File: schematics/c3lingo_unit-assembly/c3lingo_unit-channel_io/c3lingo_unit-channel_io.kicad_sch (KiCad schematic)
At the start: 40 parts, among them J601 Mic X In, J602 Headphone X, J603 Interconnect, J604 PowerSupply, J605 PhantomPower, U601 NE5534, U602 TPA6111A2

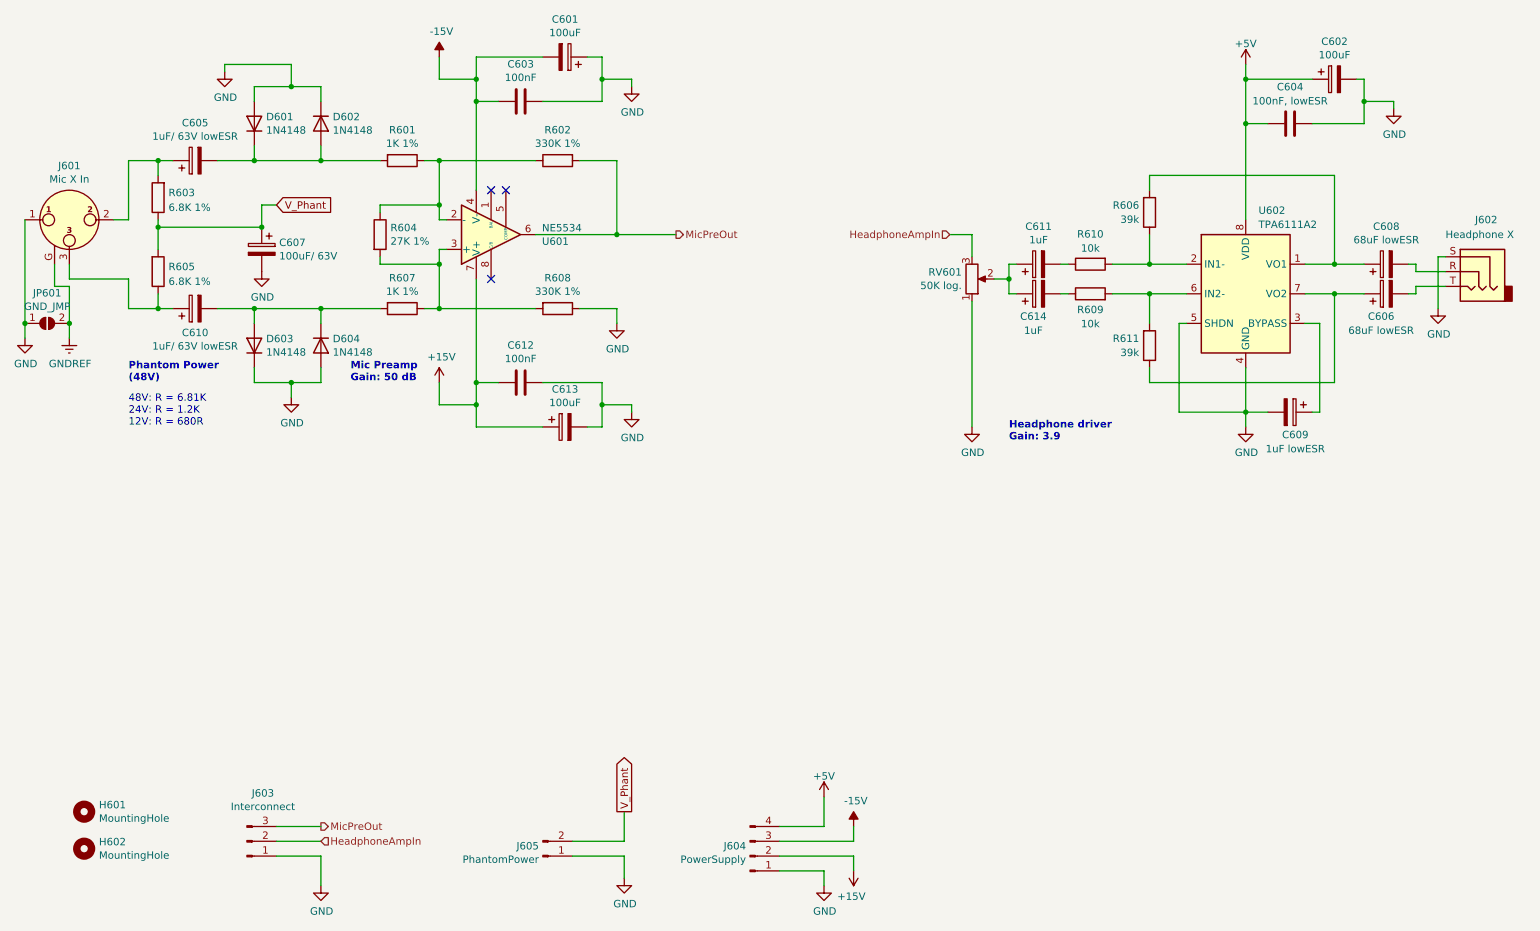
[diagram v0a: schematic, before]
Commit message: Reworks board-to-board connections
Instead of having connections between all boards, use the mix_io board as an audio signal distribution hub.

Note: PCB not updated
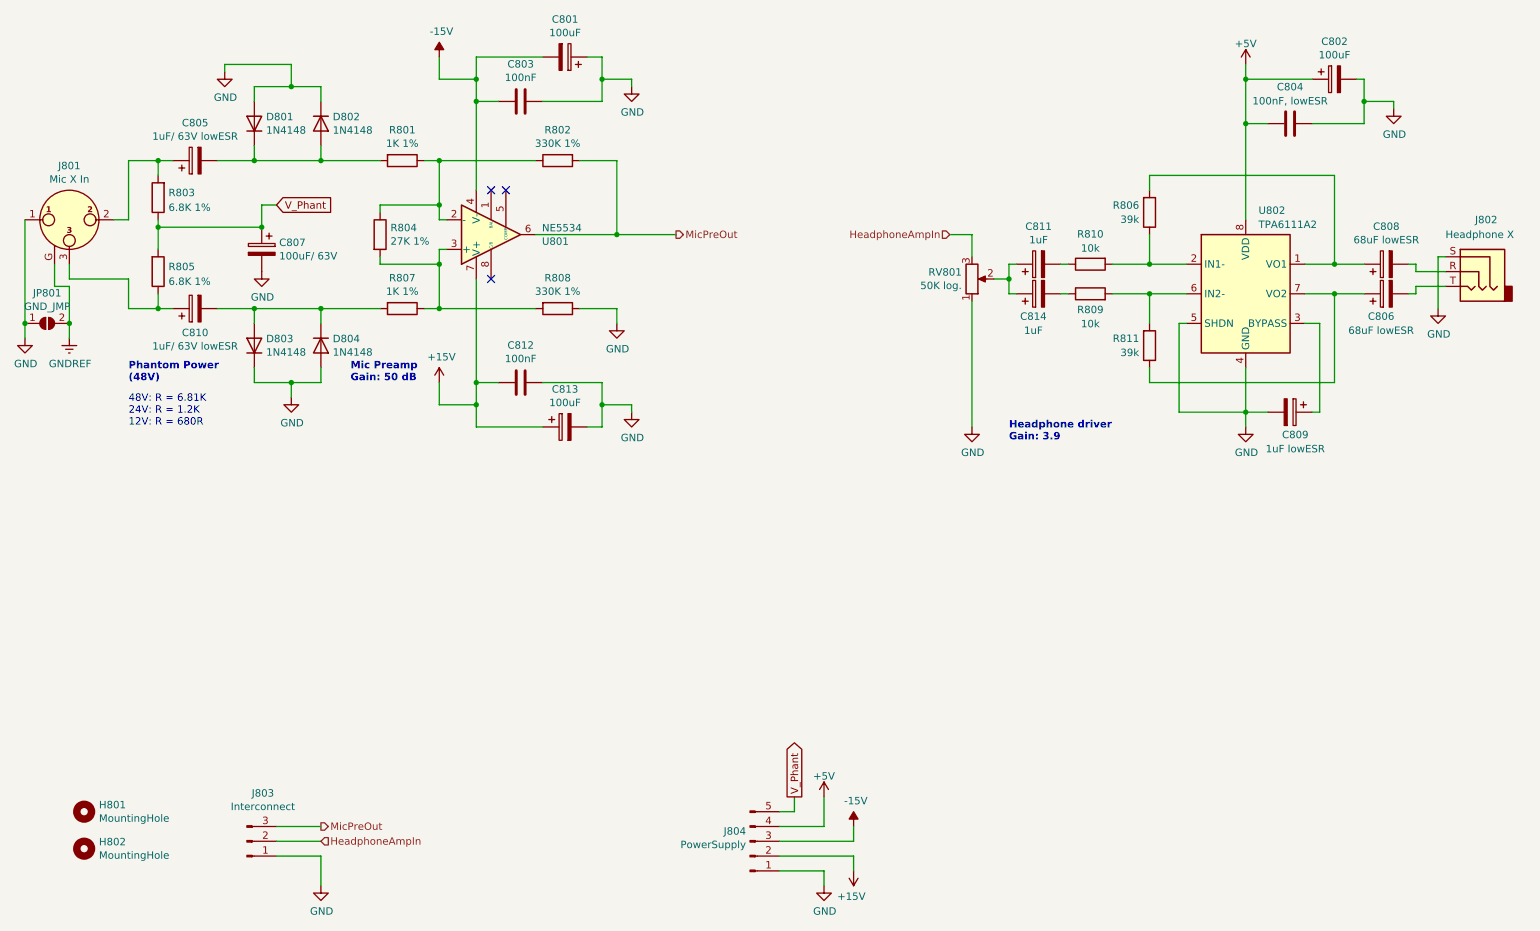
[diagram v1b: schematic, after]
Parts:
- removed J605: PhantomPower, TerminalBlock_Phoenix:TerminalBlock_Phoenix_PTSM-0,5-2-2.5-H-THR_1x02_P2.50mm_Horizontal, symbol Connector:Conn_01x02_Pin
- J803: renamed from J603; footprint TerminalBlock_Phoenix:TerminalBlock_Phoenix_PTSM-0,5-3-2.5-H-THR_1x03_P2.50mm_Horizontal -> TerminalBlock_Phoenix:TerminalBlock_Phoenix_PTSM-0,5-3-2.5-V-THR_1x03_P2.50mm_Vertical; Model PTSM 0,5/ 3-2,5-H THR -> PTSM 0,5/ 3-2,5-V THR
- J804: renamed from J604; footprint TerminalBlock_Phoenix:TerminalBlock_Phoenix_PTSM-0,5-4-2.5-H-THR_1x04_P2.50mm_Horizontal -> TerminalBlock_Phoenix:TerminalBlock_Phoenix_PTSM-0,5-5-2.5-V-THR_1x05_P2.50mm_Vertical; symbol Connector:Conn_01x04_Pin -> Connector:Conn_01x05_Pin; Model PTSM 0,5/ 4-2,5-H THR -> PTSM 0,5/ 5-2,5-V THR
- renumbered C601 to C801, C602 to C802, C603 to C803, C604 to C804, C605 to C805, C606 to C806, C607 to C807, C608 to C808, C609 to C809, C610 to C810, C611 to C811, C612 to C812, C613 to C813, C614 to C814, D601 to D801, D602 to D802, D603 to D803, D604 to D804, H601 to H801, H602 to H802, J601 to J801, J602 to J802, JP601 to JP801, R601 to R801, R602 to R802, R603 to R803, R604 to R804, R605 to R805, R606 to R806, R607 to R807, R608 to R808, R609 to R809, R610 to R810, R611 to R811, RV601 to RV801, U601 to U801, U602 to U802
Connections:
- net V_Phant: now also J804.5 (Pin_5)

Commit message: Re-layout boards with SMD components
* Channel Mix: Removed vu meter potentiometer as good setting was found (10 dB
  more headroom)
* Channel Mix: Add vu meter alternate power
* Channel I/O: Added jumper for phantom power enable/disable
* Add GND test points
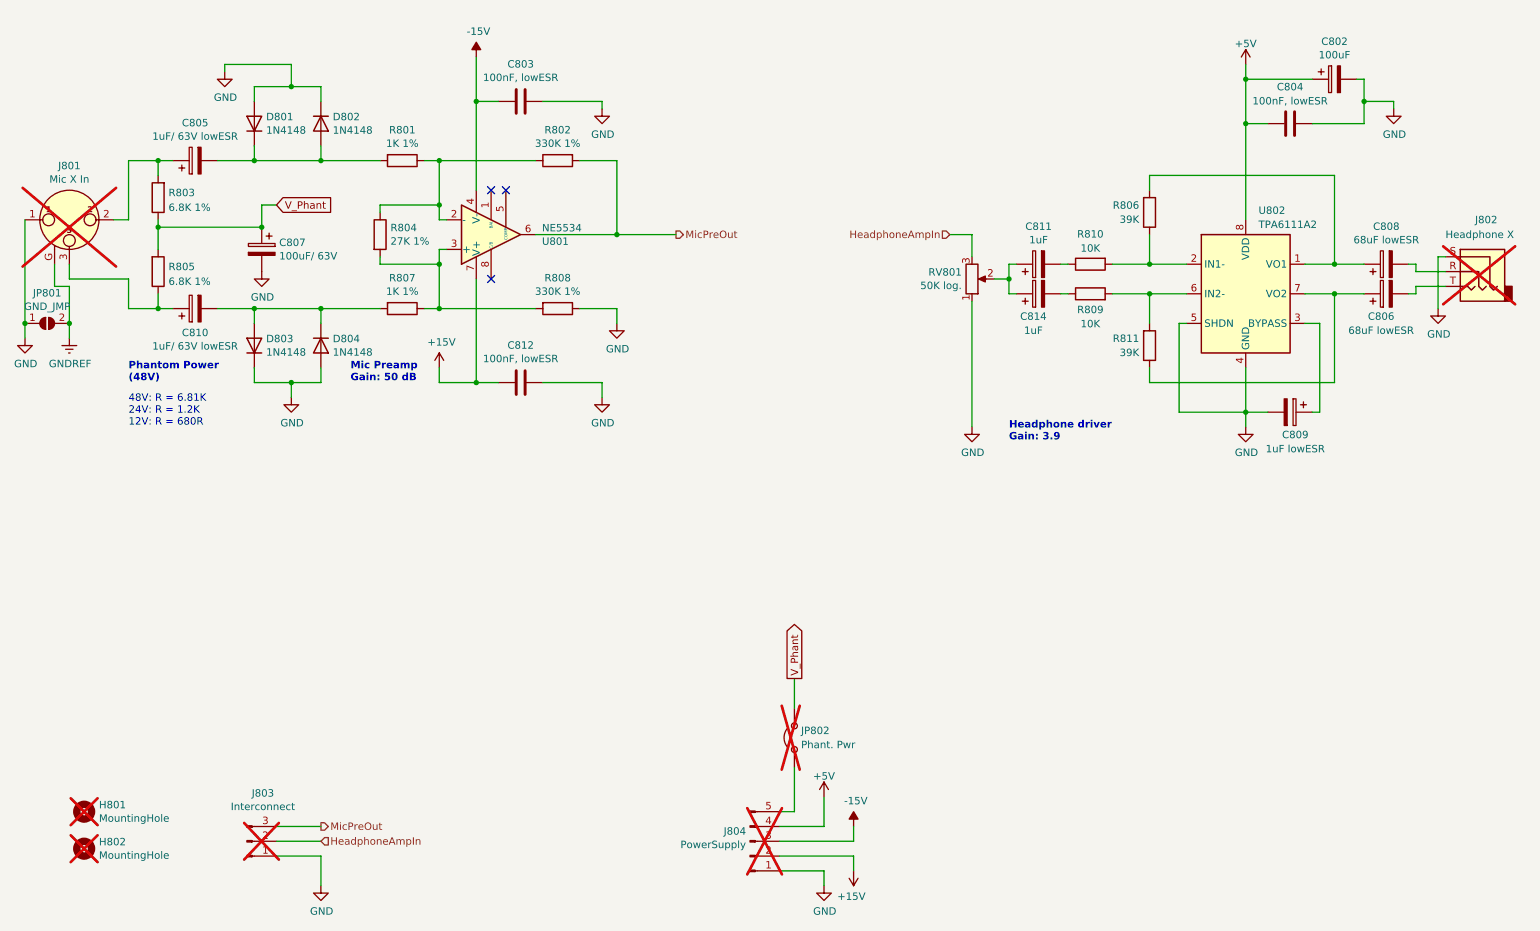
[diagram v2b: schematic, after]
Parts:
- removed C801, C813: 100uF, Capacitor_THT:CP_Radial_D6.3mm_P2.50mm, symbol Device:C_Polarized
- added JP802: Phant. Pwr, Connector_PinHeader_2.54mm:PinHeader_1x02_P2.54mm_Vertical, symbol Jumper:Jumper_2_Open
- C802: footprint Capacitor_THT:CP_Radial_D6.3mm_P2.50mm -> Capacitor_SMD:C_Elec_6.3x7.7; LCSC Part # (none) -> C72478; Model (none) -> 25V+
- C803, C812: value 100nF -> 100nF, lowESR; footprint Capacitor_THT:C_Disc_D5.0mm_W2.5mm_P5.00mm -> Capacitor_SMD:C_0603_1608Metric_Pad1.08x0.95mm_HandSolder; LCSC Part # (none) -> C14663; Model (none) -> 25V+
- C804: footprint Capacitor_THT:C_Disc_D5.0mm_W2.5mm_P5.00mm -> Capacitor_SMD:C_0603_1608Metric_Pad1.08x0.95mm_HandSolder; LCSC Part # (none) -> C14663; Model (none) -> 25V+
- C805, C810, C811, C814: footprint Capacitor_THT:CP_Radial_D5.0mm_P2.00mm -> Capacitor_SMD:C_Elec_4x5.8; LCSC Part # (none) -> C336256
- C806, C808: footprint Capacitor_THT:CP_Radial_D6.3mm_P2.50mm -> Capacitor_SMD:C_Elec_6.3x5.8; LCSC Part # (none) -> C72478
- C807: footprint Capacitor_THT:CP_Radial_D10.0mm_P5.00mm -> Capacitor_SMD:C_Elec_6.3x7.7; LCSC Part # (none) -> C72478
- C809: footprint Capacitor_THT:C_Disc_D5.0mm_W2.5mm_P5.00mm -> Capacitor_SMD:C_Elec_4x5.8; LCSC Part # (none) -> C336256
- D801, D802, D803, D804: footprint Diode_THT:D_DO-35_SOD27_P10.16mm_Horizontal -> Diode_SMD:D_SOD-123; LCSC Part # (none) -> C7420318; Model (none) -> 1N4148W (SOD-123)
- H801, H802: now not fitted; now left out of the parts list
- J801: Model NC3FAAH2 (Horiz. Male) -> NC3FAAH2 (Horiz. Female); now not fitted
- J802, J803, J804: now not fitted
- JP801: now left out of the parts list
- R801, R802, R803, R804, R805, R807, R808: footprint Resistor_THT:R_Axial_DIN0207_L6.3mm_D2.5mm_P10.16mm_Horizontal -> Resistor_SMD:R_0805_2012Metric_Pad1.20x1.40mm_HandSolder
- R806, R811: value 39k -> 39K; footprint Resistor_THT:R_Axial_DIN0207_L6.3mm_D2.5mm_P10.16mm_Horizontal -> Resistor_SMD:R_0805_2012Metric_Pad1.20x1.40mm_HandSolder
- R809, R810: value 10k -> 10K; footprint Resistor_THT:R_Axial_DIN0207_L6.3mm_D2.5mm_P10.16mm_Horizontal -> Resistor_SMD:R_0805_2012Metric_Pad1.20x1.40mm_HandSolder; LCSC Part # (none) -> C17414
- U801: footprint Package_DIP:DIP-8_W7.62mm_Socket_LongPads -> Package_SO:SOIC-8_3.9x4.9mm_P1.27mm; LCSC Part # (none) -> C9916; Model +DIP-8 Socket -> NE5534DR (SOIC-8)
- U802: LCSC Part # (none) -> C497472
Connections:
- net V_Phant: now also JP802.2 (B); no longer J804.5 (Pin_5)
- new net: J804.5 (Pin_5), JP802.1 (A)

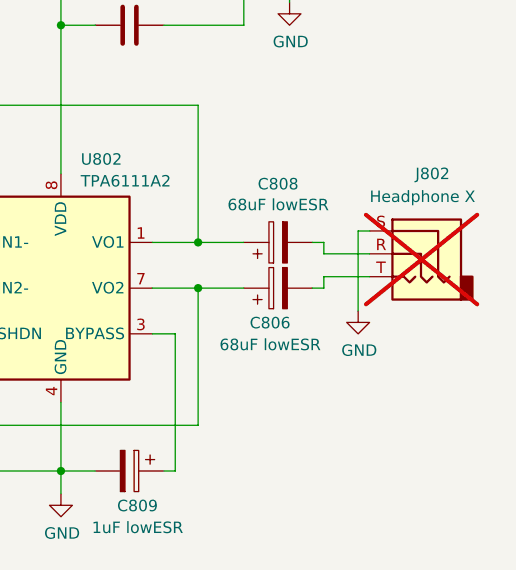
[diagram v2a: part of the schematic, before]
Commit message: Channel-Mix: Rework LED supply voltage
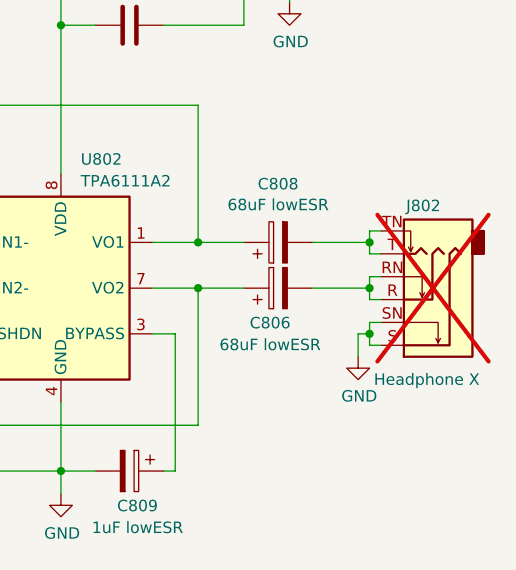
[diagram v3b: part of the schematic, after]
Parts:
- J802: symbol Connector_Audio:AudioJack3 -> Connector_Audio:NJ6FD-V
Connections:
- net GND: now also J802.SN
- net at J802.R: now also C806.2, J802.RN; no longer C808.2
- net at J802.T: now also C808.2, J802.TN; no longer C806.2
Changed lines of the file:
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@@
 	(title_block
 		(title "c3lingo interpeter unit -- channel strip (I/O)")
-		(date "2024-07-06")
+		(date "2024-07-07")
 		(rev "v0.3.0")
 		(company "Jannik Beyerstedt (jtbx)")
@@
 	)
 	(junction
+		(at 259.08 91.44)
+		(diameter 0)
+		(color 0 0 0 0)
+	)
+	(junction
 		(at 224.79 57.15)
 		(diameter 0)
@@
 	)
 	(junction
+		(at 259.08 86.36)
+		(diameter 0)
+		(color 0 0 0 0)
+	)
+	(junction
 		(at 54.61 63.5)
 		(diameter 0)
@@
 	)
 	(junction
+		(at 259.08 81.28)
+		(diameter 0)
+		(color 0 0 0 0)
+	)
+	(junction
 		(at 86.36 81.28)
 		(diameter 0)
@@
 	(wire
 		(pts
+			(xy 257.81 91.44) (xy 259.08 91.44)
+		)
+		(stroke
+			(width 0)
+			(type default)
+		)
+	)
+	(wire
+		(pts
 			(xy 54.61 88.9) (xy 54.61 91.44)
 		)
@@
 	(wire
 		(pts
+			(xy 260.35 87.63) (xy 259.08 87.63)
+		)
+		(stroke
+			(width 0)
+			(type default)
+		)
+	)
+	(wire
+		(pts
 			(xy 86.36 81.28) (xy 76.2 81.28)
 		)
@@
 	(wire
 		(pts
-			(xy 208.28 86.36) (xy 208.28 91.44)
+			(xy 260.35 85.09) (xy 259.08 85.09)
 		)
 		(stroke
@@
 	(wire
 		(pts
-			(xy 254 85.09) (xy 259.08 85.09)
+			(xy 208.28 86.36) (xy 208.28 91.44)
 		)
 		(stroke
@@
 	(wire
 		(pts
-			(xy 254 86.36) (xy 254 85.09)
+			(xy 54.61 99.06) (xy 54.61 101.6)
 		)
 		(stroke
@@
 	(wire
 		(pts
-			(xy 54.61 99.06) (xy 54.61 101.6)
+			(xy 257.81 93.98) (xy 257.81 91.44)
 		)
 		(stroke
@@
 	(wire
 		(pts
+			(xy 259.08 80.01) (xy 259.08 81.28)
+		)
+		(stroke
+			(width 0)
+			(type default)
+		)
+	)
+	(wire
+		(pts
 			(xy 144.78 177.8) (xy 152.4 177.8)
 		)
@@
 	(wire
 		(pts
+			(xy 259.08 81.28) (xy 259.08 82.55)
+		)
+		(stroke
+			(width 0)
+			(type default)
+		)
+	)
+	(wire
+		(pts
 			(xy 20.32 81.28) (xy 20.32 85.09)
 		)
@@
 	(wire
 		(pts
-			(xy 252.73 86.36) (xy 254 86.36)
+			(xy 213.36 91.44) (xy 213.36 106.68)
 		)
 		(stroke
@@
 	(wire
 		(pts
-			(xy 213.36 91.44) (xy 213.36 106.68)
+			(xy 260.35 90.17) (xy 259.08 90.17)
 		)
 		(stroke
@@
 	(wire
 		(pts
-			(xy 257.81 80.01) (xy 257.81 88.9)
+			(xy 245.11 57.15) (xy 245.11 53.34)
 		)
 		(stroke
@@
 	(wire
 		(pts
-			(xy 245.11 57.15) (xy 245.11 53.34)
+			(xy 49.53 46.99) (xy 60.96 46.99)
 		)
 		(stroke
@@
 	(wire
 		(pts
-			(xy 49.53 46.99) (xy 60.96 46.99)
+			(xy 260.35 80.01) (xy 259.08 80.01)
 		)
 		(stroke
@@
 	(wire
 		(pts
-			(xy 252.73 81.28) (xy 254 81.28)
-		)
-		(stroke
-			(width 0)
-			(type default)
-		)
-	)
-	(wire
-		(pts
-			(xy 254 82.55) (xy 259.08 82.55)
+			(xy 66.04 101.6) (xy 66.04 99.06)
 		)
 		(stroke
@@
 	(wire
 		(pts
-			(xy 66.04 101.6) (xy 66.04 99.06)
+			(xy 177.8 87.63) (xy 177.8 109.22)
 		)
 		(stroke
@@
 	(wire
 		(pts
-			(xy 177.8 87.63) (xy 177.8 109.22)
+			(xy 38.1 86.36) (xy 38.1 88.9)
 		)
 		(stroke
@@
 	(wire
 		(pts
-			(xy 38.1 86.36) (xy 38.1 88.9)
+			(xy 49.53 48.26) (xy 49.53 46.99)
 		)
 		(stroke
@@
 	(wire
 		(pts
-			(xy 49.53 48.26) (xy 49.53 46.99)
+			(xy 114.3 53.34) (xy 114.3 54.61)
 		)
 		(stroke
@@
 	(wire
 		(pts
-			(xy 114.3 53.34) (xy 114.3 54.61)
+			(xy 15.24 73.66) (xy 15.24 91.44)
 		)
 		(stroke
@@
 	(wire
 		(pts
-			(xy 15.24 73.66) (xy 15.24 91.44)
+			(xy 102.87 63.5) (xy 86.36 63.5)
 		)
 		(stroke
@@
 	(wire
 		(pts
-			(xy 102.87 63.5) (xy 86.36 63.5)
+			(xy 259.08 92.71) (xy 260.35 92.71)
 		)
 		(stroke
@@
 	(wire
 		(pts
+			(xy 252.73 81.28) (xy 259.08 81.28)
+		)
+		(stroke
+			(width 0)
+			(type default)
+		)
+	)
+	(wire
+		(pts
 			(xy 193.04 81.28) (xy 194.31 81.28)
 		)
@@
 	(wire
 		(pts
-			(xy 254 82.55) (xy 254 81.28)
+			(xy 252.73 86.36) (xy 259.08 86.36)
 		)
 		(stroke
@@
 	(wire
 		(pts
+			(xy 259.08 87.63) (xy 259.08 86.36)
+		)
+		(stroke
+			(width 0)
+			(type default)
+		)
+	)
+	(wire
+		(pts
 			(xy 66.04 182.88) (xy 58.42 182.88)
 		)
@@
 	(wire
 		(pts
+			(xy 259.08 85.09) (xy 259.08 86.36)
+		)
+		(stroke
+			(width 0)
+			(type default)
+		)
+	)
+	(wire
+		(pts
 			(xy 177.8 76.2) (xy 177.8 80.01)
 		)
@@
 	(wire
 		(pts
+			(xy 259.08 90.17) (xy 259.08 91.44)
+		)
+		(stroke
+			(width 0)
+			(type default)
+		)
+	)
+	(wire
+		(pts
 			(xy 234.95 86.36) (xy 240.03 86.36)
 		)
@@
 	(wire
 		(pts
-			(xy 86.36 73.66) (xy 87.63 73.66)
+			(xy 259.08 91.44) (xy 259.08 92.71)
 		)
 		(stroke
@@
 	(wire
 		(pts
-			(xy 237.49 91.44) (xy 237.49 106.68)
+			(xy 86.36 73.66) (xy 87.63 73.66)
 		)
 		(stroke
@@
 	(wire
 		(pts
-			(xy 22.86 81.28) (xy 22.86 83.82)
+			(xy 237.49 91.44) (xy 237.49 106.68)
 		)
 		(stroke
@@
 	(wire
 		(pts
-			(xy 54.61 50.8) (xy 60.96 50.8)
+			(xy 22.86 81.28) (xy 22.86 83.82)
 		)
 		(stroke
@@
 	(wire
 		(pts
-			(xy 257.81 80.01) (xy 259.08 80.01)
+			(xy 54.61 50.8) (xy 60.96 50.8)
 		)
 		(stroke
@@
 	(wire
 		(pts
+			(xy 259.08 82.55) (xy 260.35 82.55)
+		)
+		(stroke
+			(width 0)
+			(type default)
+		)
+	)
+	(wire
+		(pts
 			(xy 66.04 60.96) (xy 66.04 63.5)
 		)
@@
 	)
 	(symbol
-		(lib_id "Connector_Audio:AudioJack3")
-		(at 264.16 82.55 0)
-		(mirror y)
+		(lib_id "Connector_Audio:NJ6FD-V")
+		(at 265.43 87.63 180)
 		(unit 1)
 		(exclude_from_sim no)
@@
 		(dnp yes)
 		(property "Reference" "J802"
-			(at 264.16 73.66 0)
+			(at 263.144 77.216 0)
 			(effects
 				(font
@@
 		)
 		(property "Value" "Headphone X"
-			(at 259.08 76.2 0)
+			(at 265.43 96.52 0)
 			(effects
 				(font
 					(size 1.27 1.27)
 				)
-				(justify right)
 			)
 		)
 		(property "Footprint" "Connector_Audio:Jack_6.35mm_Neutrik_NMJ6HFD2_Horizontal"
-			(at 264.16 82.55 0)
+			(at 265.43 87.63 0)
 			(effects
 				(font
@@
 			)
 		)
-		(property "Datasheet" "~"
-			(at 264.16 82.55 0)
+		(property "Datasheet" ""
+			(at 265.43 87.63 0)
 			(effects
 				(font
@@
 		)
 		(property "Description" "Audio Jack, 3 Poles (Stereo / TRS)"
-			(at 264.16 82.55 0)
+			(at 265.43 87.63 0)
 			(effects
 				(font
@@
 		)
 		(property "Model" "NYS216G (Horiz.)"
-			(at 264.16 82.55 0)
+			(at 265.43 87.63 0)
 			(effects
 				(font
@@
 		(pin "T"
 		)
+		(pin "RN"
+		)
+		(pin "SN"
+		)
+		(pin "TN"
+		)
 		(instances
 			(project "c3lingo_unit-assembly"
@@
 	(symbol
 		(lib_id "power:GND")
-		(at 257.81 88.9 0)
+		(at 257.81 93.98 0)
 		(unit 1)
 		(exclude_from_sim no)
@@
 		(dnp no)
 		(property "Reference" "#PWR0812"
-			(at 257.81 95.25 0)
+			(at 257.81 100.33 0)
 			(effects
 				(font
@@
 		)
 		(property "Value" "GND"
-			(at 257.937 93.2942 0)
+			(at 257.937 98.3742 0)
 			(effects
 				(font
@@
 		)
 		(property "Footprint" ""
-			(at 257.81 88.9 0)
+			(at 257.81 93.98 0)
 			(effects
 				(font
@@
 		)
 		(property "Datasheet" ""
-			(at 257.81 88.9 0)
+			(at 257.81 93.98 0)
 			(effects
 				(font
@@
 		)
 		(property "Description" "Power symbol creates a global label with name \"GND\" , ground"
-			(at 257.81 88.9 0)
+			(at 257.81 93.98 0)
 			(effects
 				(font

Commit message: Channel I/O: Fix headphone amp caps, re-phrase readme section
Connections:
- net at R809.1: now also C814.1; no longer C814.2
- net at C811.2: now also C814.2, RV801.2; no longer R810.1
- new net: C811.1, R810.1
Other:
- moved on the sheet: C811, C814
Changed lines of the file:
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@@
 	(title_block
 		(title "c3lingo interpeter unit -- channel strip (I/O)")
-		(date "2024-07-07")
-		(rev "v0.3.0")
+		(date "2024-07-08")
+		(rev "v0.3.1")
 		(company "Jannik Beyerstedt (jtbx)")
 		(comment 1 "Prototype 2")
@@
 	(symbol
 		(lib_id "Device:C_Polarized")
-		(at 189.23 81.28 90)
+		(at 189.23 81.28 270)
 		(unit 1)
 		(exclude_from_sim no)
@@
 		(on_board yes)
 		(dnp no)
+		(fields_autoplaced yes)
 		(property "Reference" "C811"
-			(at 189.23 74.803 90)
+			(at 190.119 74.9765 90)
 			(effects
 				(font
@@
 		)
 		(property "Value" "1uF"
-			(at 189.23 77.1144 90)
+			(at 190.119 77.4008 90)
 			(effects
 				(font
@@
 		)
 		(property "Footprint" "Capacitor_SMD:C_Elec_4x5.8"
-			(at 193.04 80.3148 0)
+			(at 185.42 82.2452 0)
 			(effects
 				(font
@@
 	(symbol
 		(lib_id "Device:C_Polarized")
-		(at 189.23 86.36 90)
+		(at 189.23 86.36 270)
 		(unit 1)
 		(exclude_from_sim no)
@@
 		(fields_autoplaced yes)
 		(property "Reference" "C814"
-			(at 188.341 90.2391 90)
+			(at 190.119 90.2391 90)
 			(effects
 				(font
@@
 		)
 		(property "Value" "1uF"
-			(at 188.341 92.6633 90)
+			(at 190.119 92.6634 90)
 			(effects
 				(font
@@
 		)
 		(property "Footprint" "Capacitor_SMD:C_Elec_4x5.8"
-			(at 193.04 85.3948 0)
+			(at 185.42 87.3252 0)
 			(effects
 				(font
